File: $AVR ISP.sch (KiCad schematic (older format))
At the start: 12 parts, among them CON1 AVR-ISP-6, IC1 ATMEGA328-P, IC2 ATTINY2313-P, IC3 ATTINY85-M, IC4 ATTINY2313-S

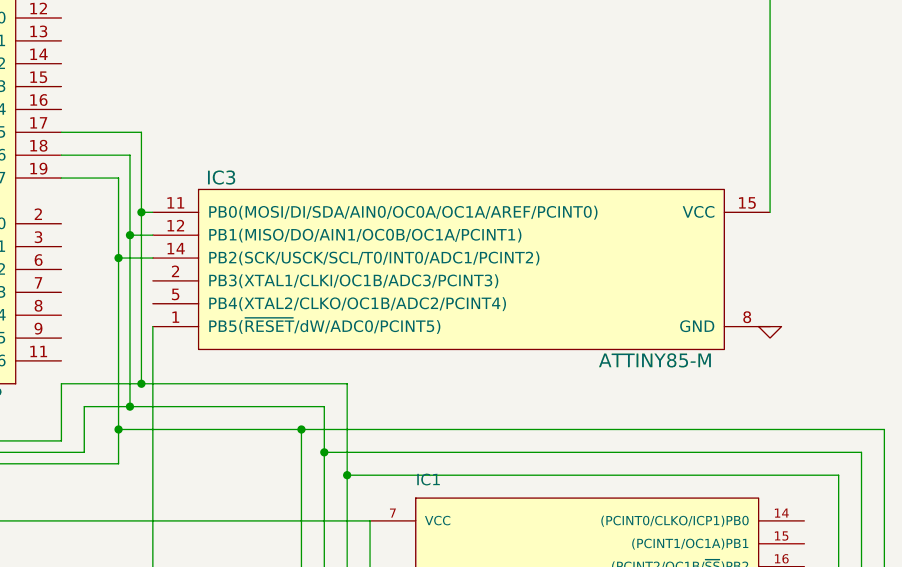
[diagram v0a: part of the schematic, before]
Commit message: Single Sided Board Layout + Footprints
Things left to do. ISP Header needs checking. Think pins are wrong. Also
need SMD Footprint for ATTiny85, possibly even a 2313 if it's a dil
style chip.
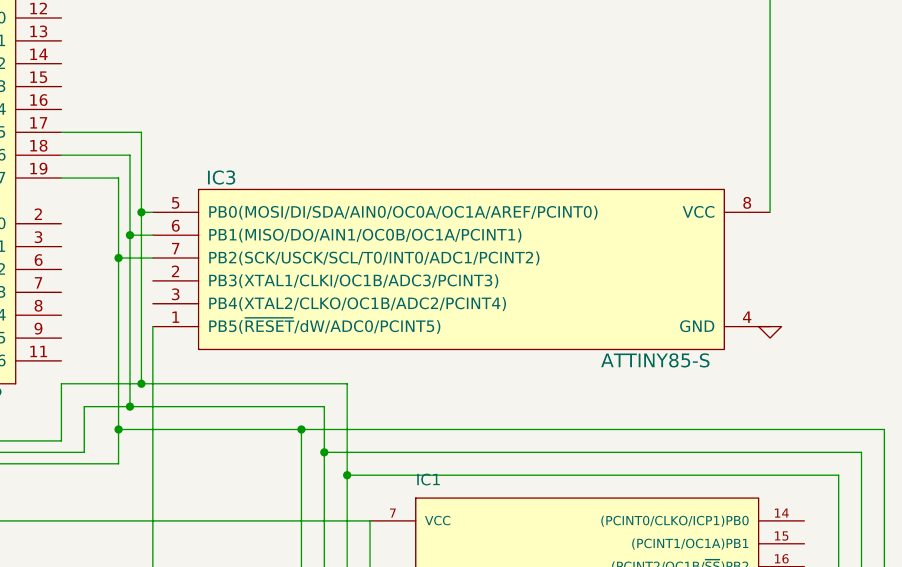
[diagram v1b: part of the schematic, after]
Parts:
- removed IC3: ATTINY85-M, QFN/MLF20, symbol ATTINY85-M
- added IC3: ATTINY85-S, SO8-200, symbol ATTINY85-S
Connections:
- net +5V: now also IC3.8 (VCC)
- net GND: now also IC3.4 (GND)
- net at CON1.5, IC1.1 ((PCINT14/~RESET~)PC6), IC2.1 (PA2(~RESET~/dW))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: now also IC3.1 (PB5(~RESET~/dW/ADC0/PCINT5))
- net at CON1.4, IC1.17 ((PCINT3/OC2A/MOSI)PB3), IC2.17 ((PCINT5/MOSI/DI/SDA)PB5)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: now also IC3.5 (PB0(MOSI/DI/SDA/AIN0/OC0A/OC1A/AREF/PCINT0))
- net at CON1.1, IC1.18 ((PCINT4/MISO)PB4), IC2.18 ((PCINT6/MISO/DO)PB6)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: now also IC3.6 (PB1(MISO/DO/AIN1/OC0B/OC1A/PCINT1))
- net at CON1.3, IC1.19 ((PCINT5/SCK)PB5), IC2.19 ((PCINT7/USCK/SCK/SCL)PB7)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: now also IC3.7 (PB2(SCK/USCK/SCL/T0/INT0/ADC1/PCINT2))
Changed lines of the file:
@@
-EESchema Schematic File Version 2  date 25/08/2013 21:04:07
+EESchema Schematic File Version 2  date 25/08/2013 21:33:02
 LIBS:power
 LIBS:device
@@
 Comment4 ""
 $EndDescr
+$Comp
+L ATTINY85-S IC3
+U 1 1 521A67A5
+P 7800 2050
+F 0 "IC3" H 7900 2100 60  0000 C CNN
+F 1 "ATTINY85-S" H 9800 1300 60  0000 C CNN
+F 2 "SO8-200" H 8050 1300 60  0001 C CNN
+	1    7800 2050
+	1    0    0    -1
+$EndComp
 Wire Wire Line
 	4975 5950 4675 5950
@@
 	1    0    0    -1
 $EndComp
-$Comp
-L ATTINY85-M IC3
-U 1 1 520B9E29
-P 7800 2050
-F 0 "IC3" H 7900 2100 60  0000 C CNN
-F 1 "ATTINY85-M" H 9800 1300 60  0000 C CNN
-F 2 "QFN/MLF20" H 8100 1300 60  0001 C CNN
-	1    7800 2050
-	1    0    0    -1
-$EndComp
